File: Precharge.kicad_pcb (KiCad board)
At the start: 2 copper layers, 79.5 x 76 mm, 22 parts, among them J1 SDC_OUT, J2 TSAL, J3 BMS, J4 SDC_IN, J5 CONN_ACC, J6 CONN_INV, J7 CONN_TSAL, K1 G2RG-2A-X DC12, K2 G2RL-1-E

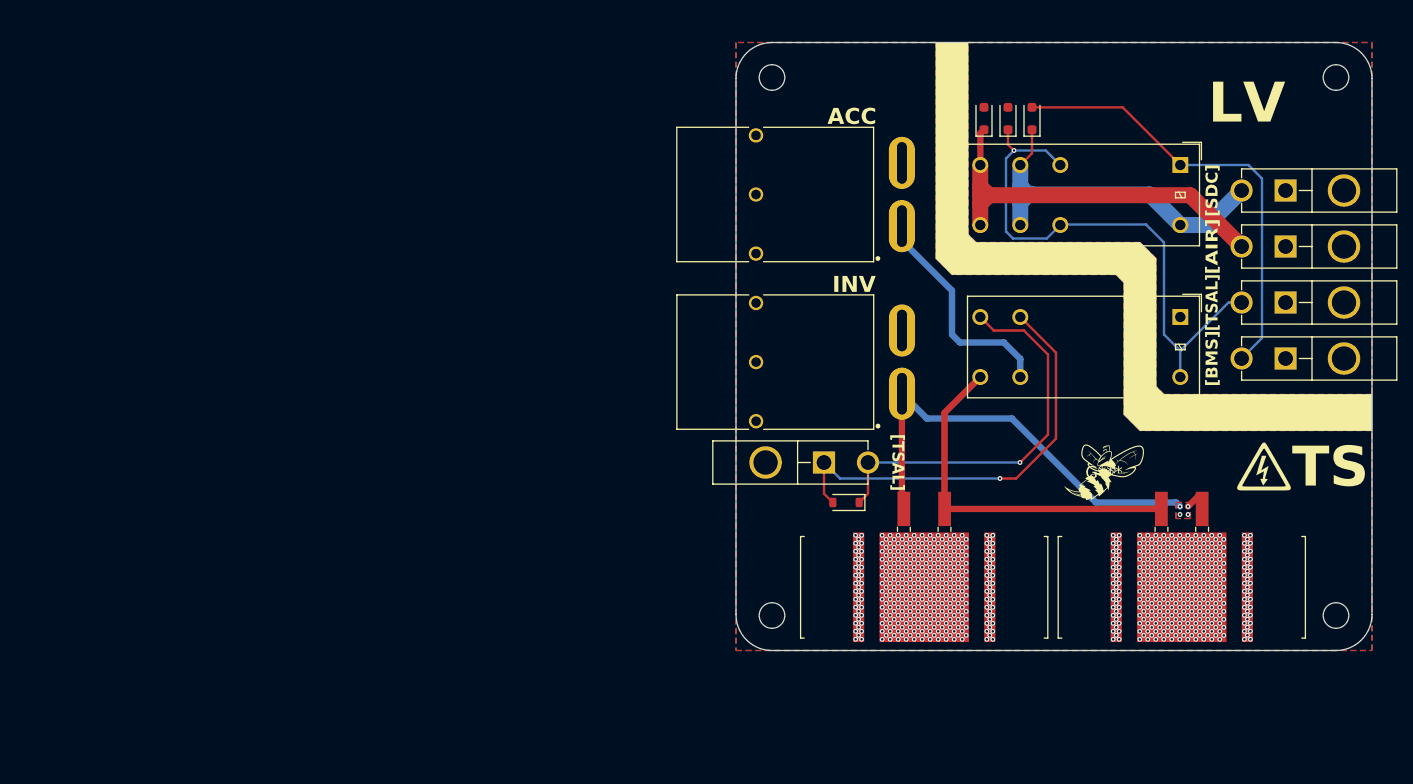
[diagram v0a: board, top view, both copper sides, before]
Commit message: New schematic
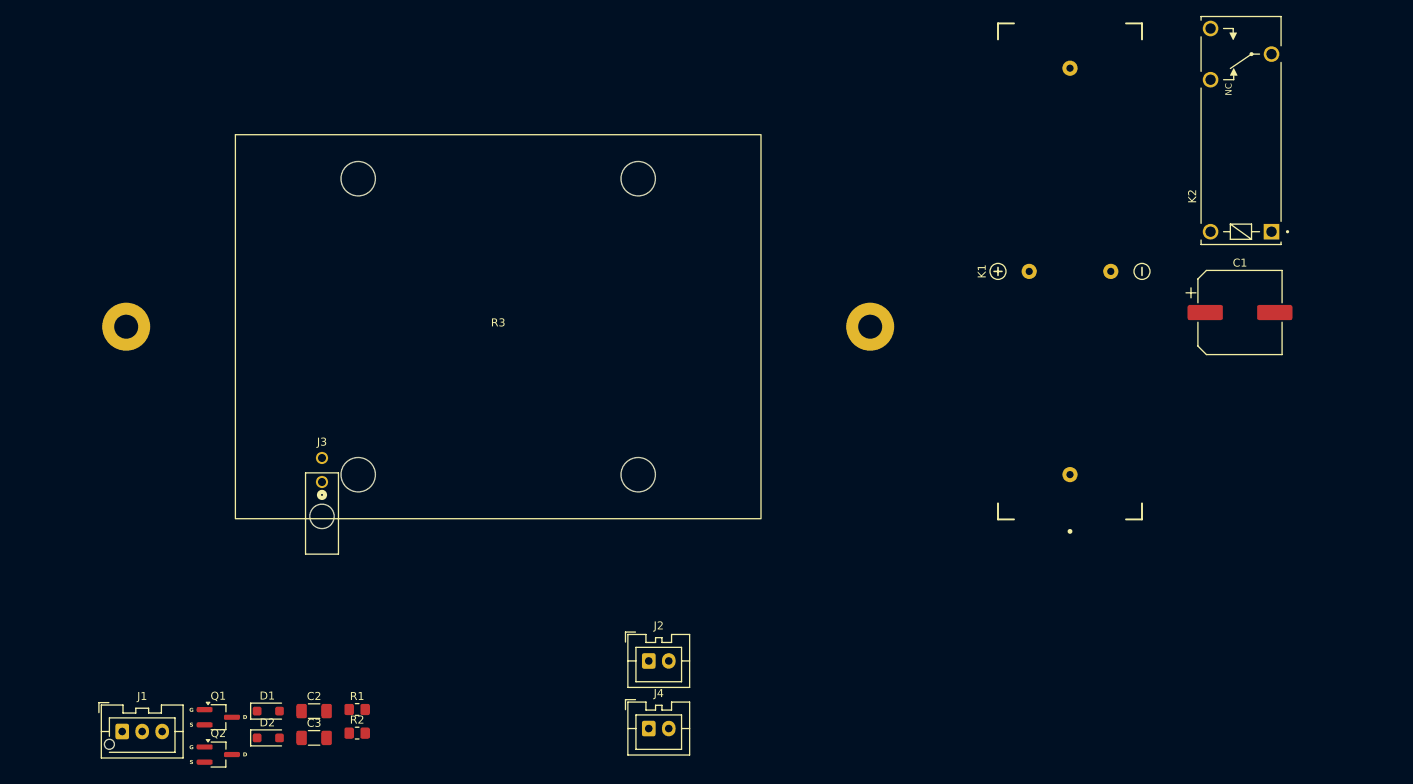
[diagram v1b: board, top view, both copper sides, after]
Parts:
- removed D3, D5: US1NWF-7, Diode_SMD:D_SOD-123F
- removed D9: D-TSAL, Diode_SMD:D_SOD-123
- removed G***: LOGO, customFootprints:stinger
- removed G*** (x2): LOGO, customFootprints:electric-shock-symbol
- removed H1 (x2), H2: HVMH, MountingHole:MountingHole_3.2mm_M3_ISO7380
- removed H3: LVMH, MountingHole:MountingHole_3.2mm_M3_ISO7380
- removed J5: CONN_ACC, customFootprints:APP_ASMPR45-1X2-RK
- removed J6: CONN_INV, customFootprints:APP_ASMPR45-1X2-RK
- removed J7: CONN_TSAL, molexMiniFitJr:MFJ_2X1
- added C1: 470u, Capacitor_SMD:CP_Elec_10x12.6, F.Cu at (232.5, 88.9)
- added C2: 10u, Capacitor_SMD:C_1206_3216Metric_Pad1.33x1.80mm_HandSolder, F.Cu at (116.8, 138.7)
- added C3: 10u, Capacitor_SMD:C_1206_3216Metric_Pad1.33x1.80mm_HandSolder, F.Cu at (116.8, 142.1)
- added D2: STPS2H100, Diode_SMD:D_SOD-123F, F.Cu at (111.0, 142.1)
- added Q1: BSS205N, Custom_MSM:MOSFET_Single_SOT-23, F.Cu at (104.8, 139.5)
- added Q2: BSS205N, Custom_MSM:MOSFET_Single_SOT-23, F.Cu at (104.8, 144.1)
- added R1: 10K, Resistor_SMD:R_0805_2012Metric_Pad1.20x1.40mm_HandSolder, F.Cu at (122.1, 138.5)
- D1: value US1NWF-7 -> STPS2H100
- J1: value SDC_OUT -> BMS_Sig; footprint molexMiniFitJr:MFJ_2X1 -> Custom_MSM:Connector_JST-XA_3POS
- J2: value TSAL -> JST-XA; footprint molexMiniFitJr:MFJ_2X1 -> Custom_MSM:Connector_JST-XA_2POS
- J3: value BMS -> MicroFit+; footprint molexMiniFitJr:MFJ_2X1 -> Custom_MSM:Connector_MicroFit-Plus_2POS
- J4: value SDC_IN -> JST-XA; footprint molexMiniFitJr:MFJ_2X1 -> Custom_MSM:Connector_JST-XA_2POS
- K1: value G2RG-2A-X DC12 -> DAR71205; footprint Relay_THT:Relay_DPST_Omron_G2RL-2A -> Custom_MSM:Relay_HV
- K2: value G2RL-1-E -> Relay_SPDT_G6RN; footprint Relay_THT:Relay_SPDT_Omron_G2RL-1-E -> Custom_MSM:Relay_SPDT_G6RN
- R2: value 10k -> 10K; footprint customFootprints:R_HS -> Resistor_SMD:R_0805_2012Metric_Pad1.20x1.40mm_HandSolder
- R3: value 10k -> 3.3K; footprint customFootprints:R_HS -> customFootprints:HS100
- moved J1 157.6 mm to (92.8, 141.2), turned to 0 degrees
- moved J3 121.4 mm to (117.8, 110.1), turned to 0 degrees
- moved D1 118.5 mm to (111.0, 138.7), turned to 0 degrees
- moved J4 104.2 mm to (158.6, 140.9), turned to 0 degrees
- moved R3 91.4 mm to (139.8, 90.7), turned to 0 degrees
- moved J2 91.3 mm to (158.6, 132.4), turned to 0 degrees
- moved R2 73.2 mm to (122.1, 141.4), turned to 0 degrees
- moved K1 14.9 mm to (211.2, 83.7), turned to 90 degrees
- moved K2 14.1 mm to (236.4, 78.8), turned to 90 degrees
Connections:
- D1 pad 1: /CHARGE_COIL -> LVS
- D1 pad 2: LVGND -> Net-(D1-A)
- J1 pad 1: LVGND -> /PC_En
- J1 pad 2: /AIR_COIL -> /SDC_En
- J2 pad 1: LVGND -> LVS
- J2 pad 2: /CHARGE_COIL -> GND
- J3 pad 1: LVGND -> VEH+
- J3 pad 2: /BMS_SIG -> BATT+
- J4 pad 1: LVGND -> /SDC_Conn1
- J4 pad 2: SDC_IN -> /SDC_Conn2
- R2 pad 1: /ACC_SW -> LVS
- R2 pad 2: INV+ -> /SDC_En
- R3 pad 1: INV+ -> VEH+
- R3 pad 2: /ACC_SW -> Net-(R3--)
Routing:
- net /CHARGE_COIL: track 69.6 -> 0.00 mm, vias 1 -> 0
- net INV+: track 61.5 -> 0.00 mm, vias 4 -> 0
- net /BMS_SIG: track 56.0 -> 0.00 mm
- net /TSAL_SW+: track 54.4 -> 0.00 mm, vias 1 -> 0
- net /TSAL_SW-: track 49.8 -> 0.00 mm, vias 1 -> 0
- net /AIR_COIL: track 49.4 -> 0.00 mm
- net SDC_IN: track 46.8 -> 0.00 mm
- net /ACC_SW: track 45.5 -> 0.00 mm
- net ACC+: track 28.2 -> 0.00 mm
- net ACC-: vias 758 -> 0
- removed copper zone on B.Cu, net ACC-
- removed copper zone on F.Cu, net ACC-
- removed copper zone on B.Cu, net INV+
- removed copper zone on F.Cu, net INV+
- removed copper zone on B.Cu, net LVGND
- removed copper zone on F.Cu, net LVGND
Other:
- board outline removed
- board text removed: "10k"
- board text removed: "ACC"
- board text removed: "INV"
- board text removed: "LV"
- board text removed: "R3"
- board text removed: "TS"
- board text removed: "[AIR]"
- board text removed: "[BMS]"
- board text removed: "[SDC]"
- board text removed: "[TSAL]"

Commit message: Finished schematic and PCB
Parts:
- removed the C3 at (116.8, 142.1)
- removed the J1 at (92.8, 141.2)
- added C1: 10u, Capacitor_SMD:C_1206_3216Metric_Pad1.33x1.80mm_HandSolder, F.Cu at (129.0, 100.1)
- added J3: BMS_Sig, Custom_MSM:Connector_JST-XA_3POS, F.Cu at (89.9, 79.1)
- added R10: 97.6K, Resistor_SMD:R_0805_2012Metric_Pad1.20x1.40mm_HandSolder, F.Cu at (113.0, 69.4)
- added R11: 105K, Resistor_SMD:R_0805_2012Metric_Pad1.20x1.40mm_HandSolder, F.Cu at (125.5, 71.9)
- added R12: 105K, Resistor_SMD:R_0805_2012Metric_Pad1.20x1.40mm_HandSolder, F.Cu at (113.0, 66.9)
- added R13: 20K, Resistor_SMD:R_0805_2012Metric_Pad1.20x1.40mm_HandSolder, F.Cu at (125.2, 106.4)
- added R14: 10K, Resistor_SMD:R_0805_2012Metric_Pad1.20x1.40mm_HandSolder, F.Cu at (127.8, 93.9)
- added R15: 97.6K, Resistor_SMD:R_0805_2012Metric_Pad1.20x1.40mm_HandSolder, F.Cu at (122.8, 93.9)
- added R16: 105K, Resistor_SMD:R_0805_2012Metric_Pad1.20x1.40mm_HandSolder, F.Cu at (120.2, 93.9)
- added R17: 105K, Resistor_SMD:R_0805_2012Metric_Pad1.20x1.40mm_HandSolder, F.Cu at (127.8, 106.4)
- added R18: 97.6K, Resistor_SMD:R_0805_2012Metric_Pad1.20x1.40mm_HandSolder, F.Cu at (122.8, 106.4)
- added R19: 105K, Resistor_SMD:R_0805_2012Metric_Pad1.20x1.40mm_HandSolder, F.Cu at (125.2, 93.9)
- added R20: 105K, Resistor_SMD:R_0805_2012Metric_Pad1.20x1.40mm_HandSolder, F.Cu at (120.2, 106.4)
- added R4: 5K, Package_TO_SOT_SMD:TO-263-2, F.Cu at (176.0, 99.1)
- added R5: 20K, Resistor_SMD:R_0805_2012Metric_Pad1.20x1.40mm_HandSolder, F.Cu at (113.0, 71.9)
- added R6: 10K, Resistor_SMD:R_0805_2012Metric_Pad1.20x1.40mm_HandSolder, F.Cu at (125.5, 74.4)
- added R7: 97.6K, Resistor_SMD:R_0805_2012Metric_Pad1.20x1.40mm_HandSolder, F.Cu at (125.5, 66.9)
- added R8: 105K, Resistor_SMD:R_0805_2012Metric_Pad1.20x1.40mm_HandSolder, F.Cu at (125.5, 69.4)
- added R9: 105K, Resistor_SMD:R_0805_2012Metric_Pad1.20x1.40mm_HandSolder, F.Cu at (113.0, 74.4)
- added REF**: Board_Medium_Outer-Mounting, Custom_MSM:Board_Medium_Outer-Mounting, F.Cu at (139.1, 102.6)
- added U1: TLV1702, Custom_MSM:Comparator_Dual_VSSOP-8, F.Cu at (119.2, 70.6)
- added U2: TLV1702, Custom_MSM:Comparator_Dual_VSSOP-8, F.Cu at (124.0, 100.1)
- J2: value JST-XA -> SDC_IO
- J4: value JST-XA -> LVS
- R1, R2: value 10K -> 5K; footprint Resistor_SMD:R_0805_2012Metric_Pad1.20x1.40mm_HandSolder -> Package_TO_SOT_SMD:TO-263-2
- R3: value 3.3K -> 5K; footprint customFootprints:HS100 -> Package_TO_SOT_SMD:TO-263-2
- moved K2 136.9 mm to (99.6, 76.5), turned to -90 degrees
- moved C3 131.9 mm to (103.0, 114.1), turned to 90 degrees
- moved J2 77.7 mm to (89.9, 96.1), turned to -90 degrees
- moved Q2 75.8 mm to (94.0, 69.1), turned to -90 degrees
- moved J1 75.5 mm to (188.5, 83.6), turned to 90 degrees
- moved J4 73.4 mm to (89.9, 115.1), turned to -90 degrees
- moved D2 72.5 mm to (102.0, 70.1), turned to 180 degrees
- moved R1 69.6 mm to (190.0, 123.1), turned to -90 degrees
- moved C2 69.1 mm to (108.0, 70.1), turned to 90 degrees
- moved K1 63.1 mm to (151.0, 102.6)
- moved R2 56.9 mm to (176.0, 123.1), turned to -90 degrees
- moved R3 50.9 mm to (190.0, 99.1), turned to 90 degrees
- moved D1 44.9 mm to (134.0, 100.1), turned to -90 degrees
- moved Q1 42.8 mm to (134.0, 108.1), turned to 90 degrees
- renumbered C1 to C3, J3 to J1
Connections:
- J2 pad 1: LVS -> /SDC_1
- J2 pad 2: GND -> /SDC_2
- J4 pad 1: /SDC_Conn1 -> LVS
- J4 pad 2: /SDC_Conn2 -> GND
- K1 pad 1: Net-(R3--) -> Net-(K1-Pad1)
- K2 pad 2: /SDC_Conn2 -> /SDC_2
- K2 pad 3: /SDC_Conn1 -> /SDC_1
- Q1 pad 1: /PC_En -> /PC_Gate
- Q2 pad 1: /SDC_En -> /SDC_Gate
- R1 pad 1: LVS -> VEH+
- R1 pad 2: /PC_En -> VEH+
- R2 pad 1: LVS -> VEH+
- R2 pad 2: /SDC_En -> VEH+
- R3 pad 1: VEH+ -> Net-(R1-Pad3)
- R3 pad 2: Net-(R3--) -> VEH+
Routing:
- net LVS: track 0.00 -> 219.1 mm, vias 0 -> 6
- net Net-(K1-Pad1): track 0.00 -> 66.1 mm, vias 0 -> 16
- net /PC_En: track 0.00 -> 46.2 mm
- net /SDC_En: track 0.00 -> 42.7 mm
- net BATT+: track 0.00 -> 37.2 mm
- net /SDC_Gate: track 0.00 -> 35.9 mm, vias 0 -> 2
- net Net-(D1-A): track 0.00 -> 28.6 mm
- net /PC_Gate: track 0.00 -> 24.1 mm, vias 0 -> 2
- net /SDC_1: track 0.00 -> 19.7 mm
- net Net-(U2A--): track 0.00 -> 13.4 mm
- net Net-(U1A--): track 0.00 -> 13.4 mm
- net Net-(D2-A): track 0.00 -> 12.5 mm
- net /SDC_2: track 0.00 -> 9.61 mm
- net Net-(U2B--): track 0.00 -> 9.35 mm
- net Net-(U1B--): track 0.00 -> 9.35 mm
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- added copper zone on B.Cu, net GND
- added copper zone on F.Cu, net GND
- added copper zone on B.Cu, net Net-(K1-Pad1)
- added copper zone on F.Cu, net Net-(K1-Pad1)
- added copper zone on B.Cu, net VEH+
- added copper zone on F.Cu, net VEH+
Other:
- board outline added: 118 x 78 mm
- board text added: "4mm"
- board text added: "Isolation"

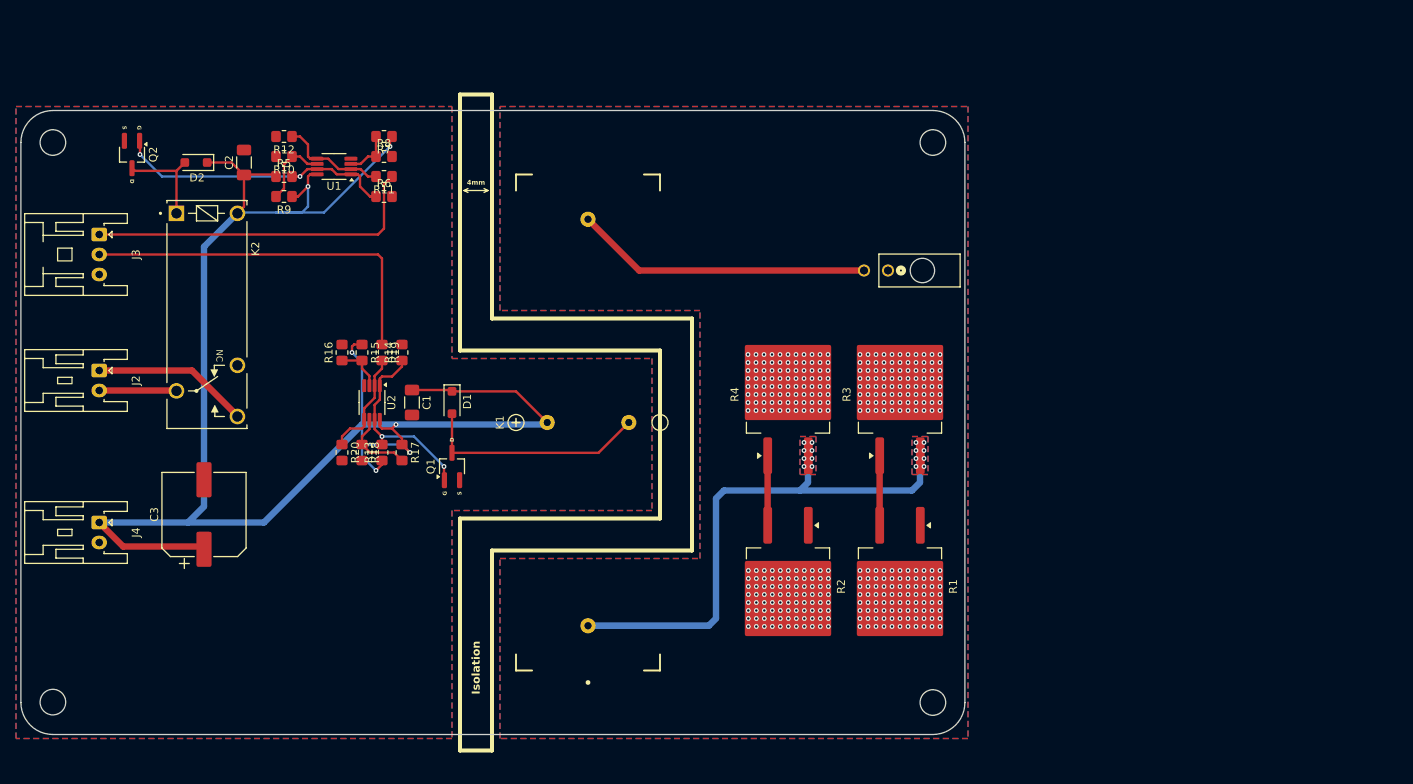
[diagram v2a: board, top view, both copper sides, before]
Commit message: Downsized to extra small
New relay, longer precharge time, option to shorten and add parallel resistors for lower load
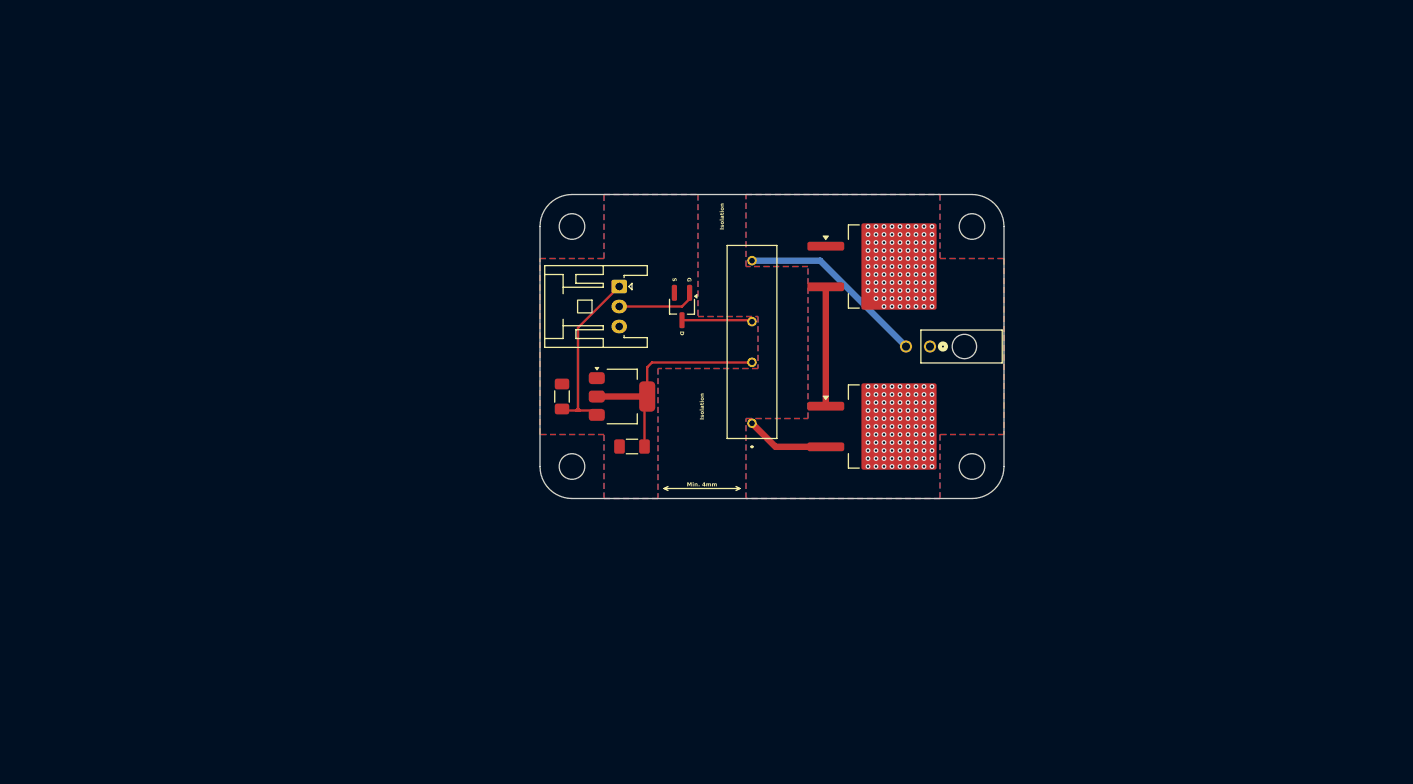
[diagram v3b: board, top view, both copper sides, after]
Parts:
- removed C3: 470u, Capacitor_SMD:CP_Elec_10x12.6
- removed D1, D2: STPS2H100, Diode_SMD:D_SOD-123F
- removed J3: BMS_Sig, Custom_MSM:Connector_JST-XA_3POS
- removed J4: LVS, Custom_MSM:Connector_JST-XA_2POS
- removed K2: Relay_SPDT_G6RN, Custom_MSM:Relay_SPDT_G6RN
- removed Q2: BSS205N, Custom_MSM:MOSFET_Single_SOT-23
- removed R10, R15, R18, R7: 97.6K, Resistor_SMD:R_0805_2012Metric_Pad1.20x1.40mm_HandSolder
- removed R11, R12, R16, R17, R19, R20, R8, R9: 105K, Resistor_SMD:R_0805_2012Metric_Pad1.20x1.40mm_HandSolder
- removed R13, R5: 20K, Resistor_SMD:R_0805_2012Metric_Pad1.20x1.40mm_HandSolder
- removed R14, R6: 10K, Resistor_SMD:R_0805_2012Metric_Pad1.20x1.40mm_HandSolder
- removed R2, R4: 5K, Package_TO_SOT_SMD:TO-263-2
- removed the REF** at (139.1, 102.6)
- removed U2: TLV1702, Custom_MSM:Comparator_Dual_VSSOP-8
- added REF**: Board_XSmall_Outer-Mounting, Library:Board_XSmall_Outer-Mounting, F.Cu at (174.0, 93.1)
- C1, C2: footprint Capacitor_SMD:C_1206_3216Metric_Pad1.33x1.80mm_HandSolder -> Library:C_1206_3216Metric_Pad1.33x1.80mm_HandSolder
- J1: footprint Custom_MSM:Connector_MicroFit-Plus_2POS -> Library:Connector_MicroFit-Plus_2POS
- J2: value SDC_IO -> JST-XA; footprint Custom_MSM:Connector_JST-XA_2POS -> Library:Connector_JST-XA_3POS
- K1: footprint Custom_MSM:Relay_HV -> Library:Relay_HV
- Q1: footprint Custom_MSM:MOSFET_Single_SOT-23 -> Library:MOSFET_Single_SOT-23
- R1, R3: footprint Package_TO_SOT_SMD:TO-263-2 -> Library:TO-263-2
- U1: value TLV1702 -> NCP1117; footprint Custom_MSM:Comparator_Dual_VSSOP-8 -> Library:Regulator_Linear_SOT-223-4
- moved J2 65.8 mm to (154.9, 85.6)
- moved C2 60.1 mm to (156.5, 105.6), turned to 0 degrees
- moved U1 46.1 mm to (155.2, 99.4), turned to 0 degrees
- moved R1 40.0 mm to (188.4, 83.1), turned to 0 degrees
- moved Q1 35.0 mm to (162.8, 88.1), turned to -90 degrees
- moved K1 22.6 mm to (171.5, 93.1)
- moved C1 18.8 mm to (147.8, 99.4)
- moved J1 10.9 mm to (193.8, 93.1)
- moved R3 4.32 mm to (188.4, 103.1), turned to 0 degrees
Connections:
- C1 pad 1: LVS -> GND
- C1 pad 2: GND -> LVS
- C2 pad 1: LVS -> GND
- C2 pad 2: GND -> +12VREG
- J2 pad 1: /SDC_1 -> LVS
- J2 pad 2: /SDC_2 -> /PC_En
- K1 pad 2: BATT+ -> +12VREG
- K1 pad 4: LVS -> BATT+
- Q1 pad 1: /PC_Gate -> /PC_En
- U1 pad 1: /SDC_Gate -> GND
- U1 pad 2: Net-(U1A--) -> +12VREG
- U1 pad 3: Net-(U1A-+) -> LVS
- U1 pad 4: GND -> +12VREG
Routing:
- net LVS: track 219.1 -> 23.0 mm, vias 6 -> 0
- net Net-(K1-Pad1): track 66.1 -> 10.4 mm, vias 16 -> 0
- net /SDC_En: track 42.7 -> 0.00 mm
- net /PC_En: track 46.2 -> 9.95 mm
- net /SDC_Gate: track 35.9 -> 0.00 mm, vias 2 -> 0
- net +12VREG: track 0.00 -> 29.7 mm
- net /PC_Gate: track 24.1 -> 0.00 mm, vias 2 -> 0
- net Net-(Q1-D): track 28.6 -> 8.83 mm
- net /SDC_1: track 19.7 -> 0.00 mm
- net BATT+: track 37.2 -> 23.7 mm
- net Net-(U2A--): track 13.4 -> 0.00 mm
- net Net-(U1A--): track 13.4 -> 0.00 mm
- net Net-(D2-A): track 12.5 -> 0.00 mm
- net /SDC_2: track 9.61 -> 0.00 mm
- net Net-(U2B--): track 9.35 -> 0.00 mm
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- removed copper zone on B.Cu, net Net-(K1-Pad1)
- removed copper zone on F.Cu, net Net-(K1-Pad1)
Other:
- board size 118 x 78 mm -> 58 x 38 mm
- board text added: "Min. 4mm"
- board text removed: "4mm"
